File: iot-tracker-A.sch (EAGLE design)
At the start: 24 parts, among them IC1 ESP-WROOM-02, IC2 TPS610986DSER, U1 TPL5111DDCR

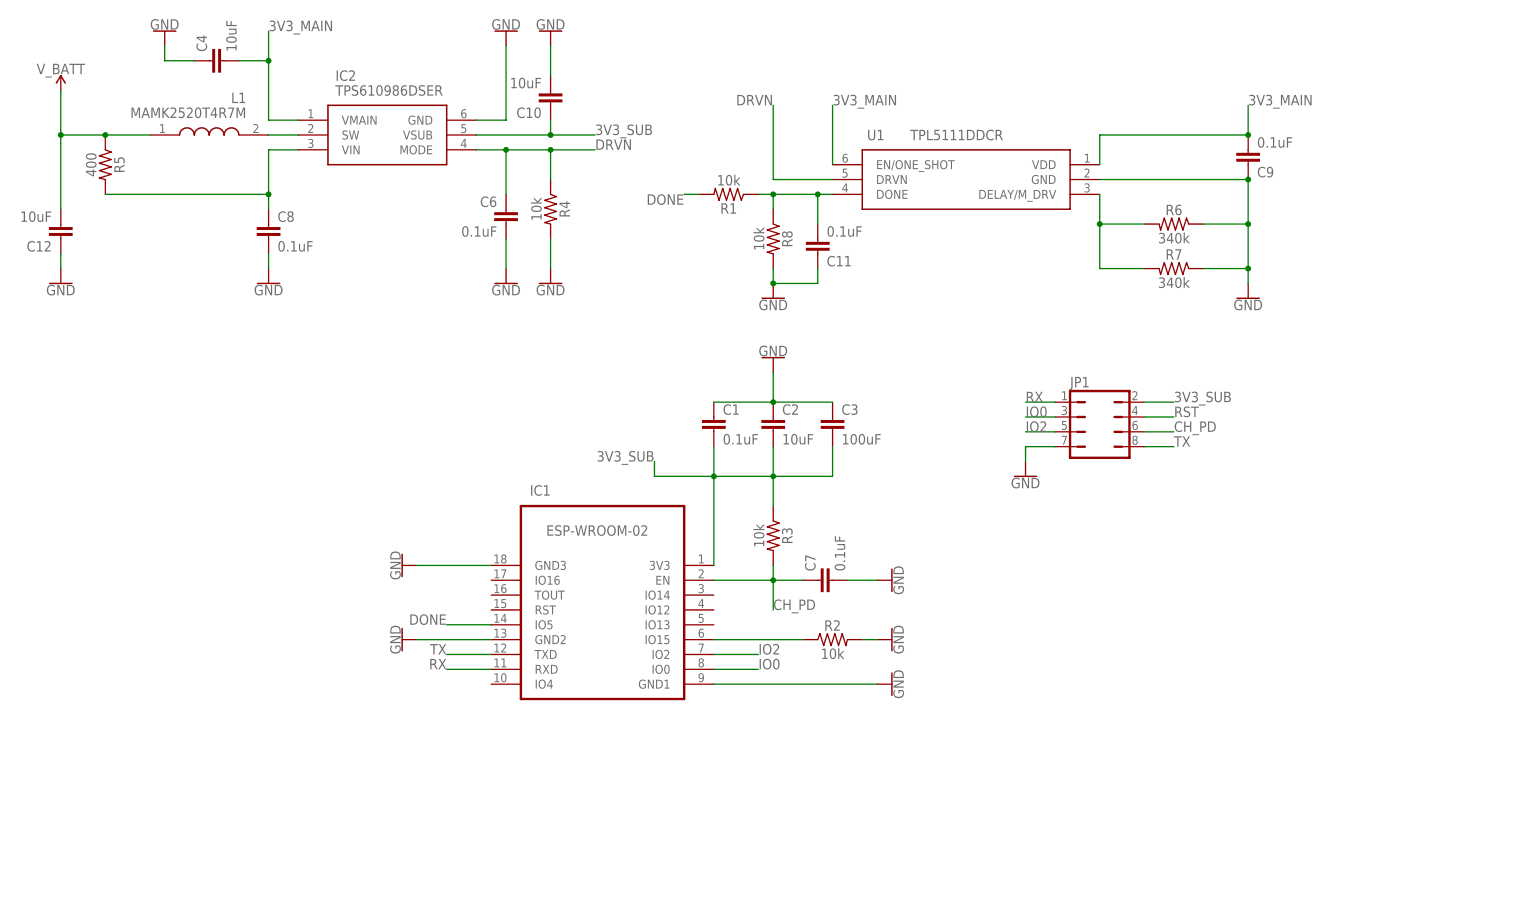
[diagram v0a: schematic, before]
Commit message: Added LED to GPIO4.
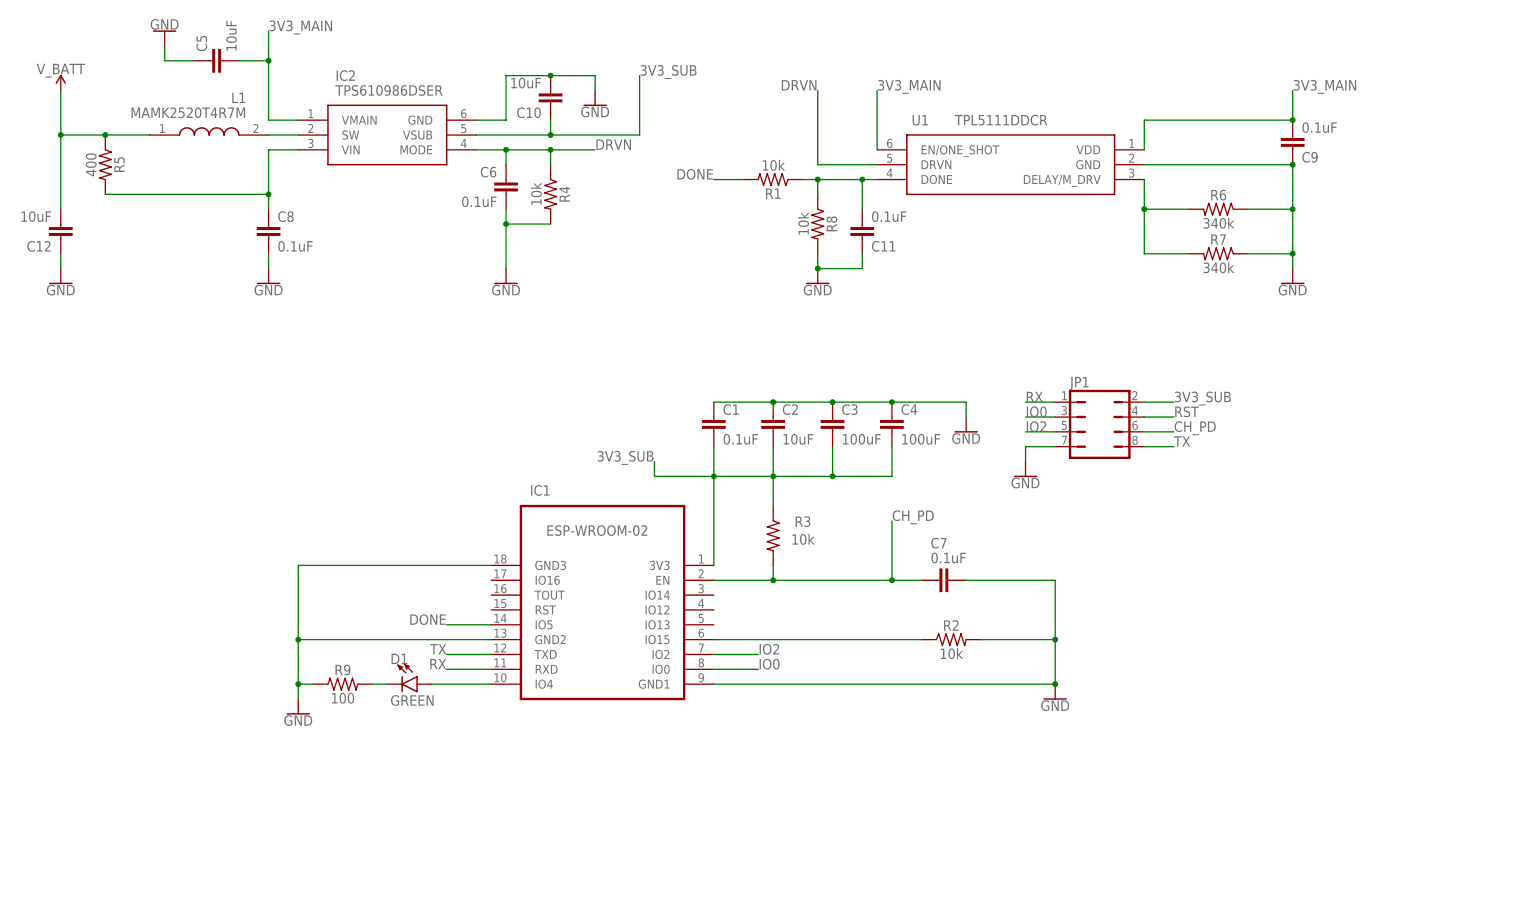
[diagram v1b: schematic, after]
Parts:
- added C5: 10uF, SparkFun-Capacitors:10UF-0603-6.3V-20%
- added D1: GREEN, SparkFun-LED:LED-GREEN0603
- added R9: 100, SparkFun-Resistors:100OHM-0603-1/10W-1%
- C4: value 10uF -> 100uF; device SparkFun-Capacitors:10UF-0603-6.3V-20% -> SparkFun-Capacitors:10UF-1206-6.3V-20%
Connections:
- new net N$2: D1.A, IC1.IO4
- new net N$5: D1.C, R9.2
- net 3V3_MAIN: now also C5.2; no longer C4.2
- net 3V3_SUB: now also C4.2
- net CH_PD: now also C7.2; no longer C7.1
- net GND: now also C5.1, C7.1, R9.1; no longer C7.2
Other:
- moved on the sheet: C11, C4, C6, C7, C9, R1, R2, R4, R6, R7, R8, U1

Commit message: Replaced TPS610986 with MCP1640 boost converter
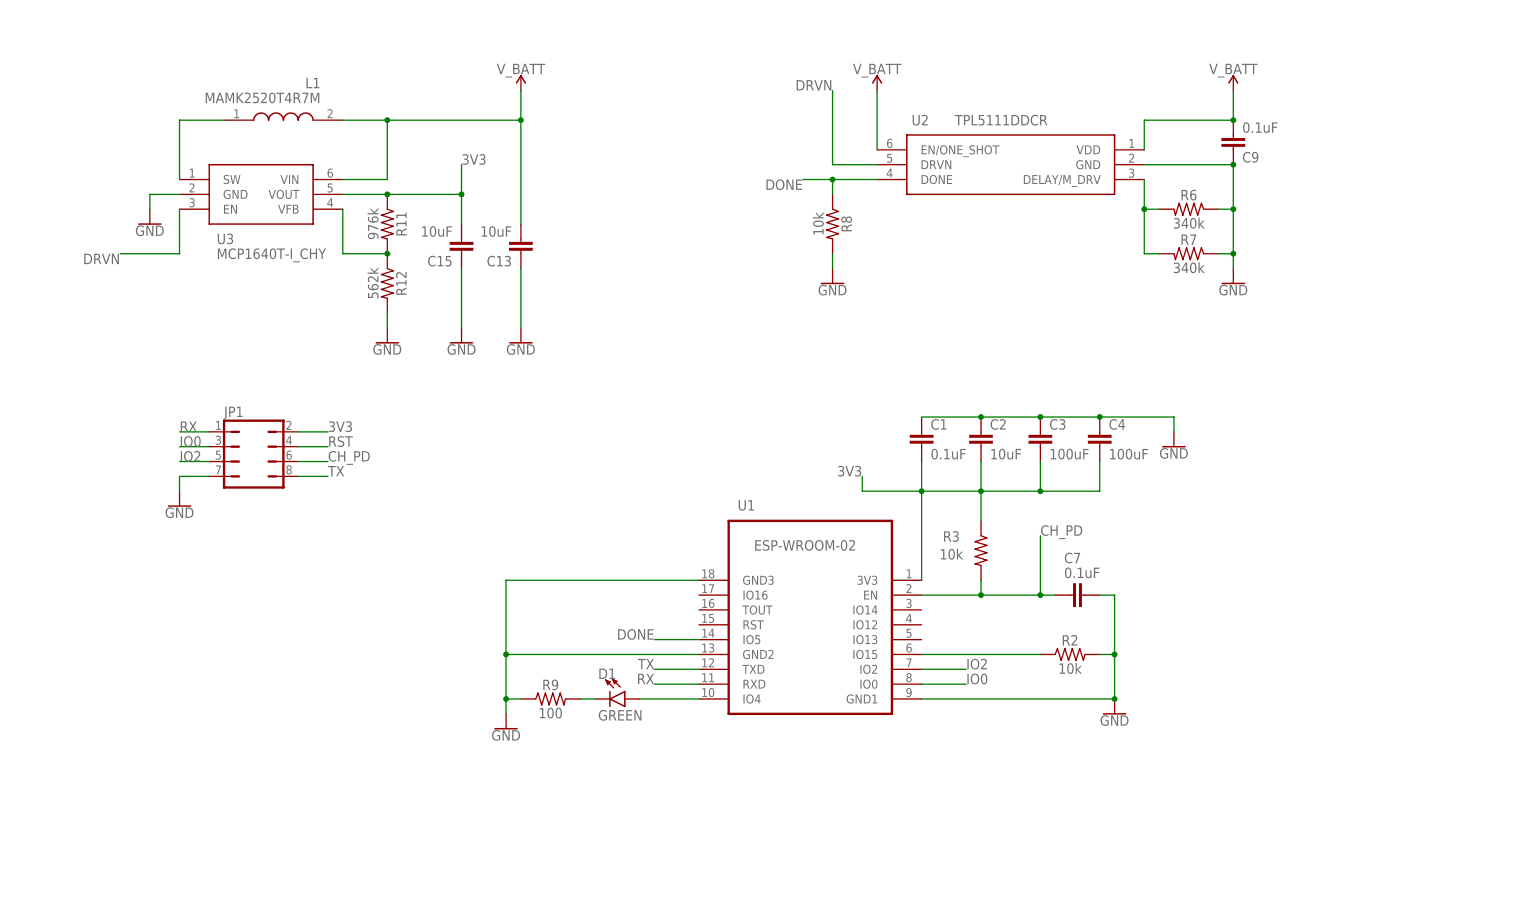
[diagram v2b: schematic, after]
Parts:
- removed C10, C12, C5: 10uF, SparkFun-Capacitors:10UF-0603-6.3V-20%
- removed C11, C6, C8: 0.1uF, SparkFun-Capacitors:0.1UF-0603-25V-(+80/-20%)
- removed IC1: ESP-WROOM-02, esp-wroom-02:ESP-WROOM-02
- removed IC2: TPS610986DSER, TPS610986DSER:TPS610986DSER
- removed R1, R4: 10k, SparkFun-Resistors:10KOHM-0603-1/10W-1%
- removed R5: 400, SparkFun-Resistors:10KOHM-0603-1/10W-1%
- added C13, C15: 10uF, SparkFun-Capacitors:10UF-0603-6.3V-20%
- added R11: 976k, SparkFun-Resistors:680OHM-0603-1/10W-5%
- added R12: 562k, SparkFun-Resistors:680OHM-0603-1/10W-5%
- added U2: TPL5111DDCR, TPL5111DDCR:TPL5111DDCR
- added U3: MCP1640T-I_CHY, MCP1640T-I_CHY:MCP1640T-I_CHY
- U1: value TPL5111DDCR -> ESP-WROOM-02; device TPL5111DDCR:TPL5111DDCR -> esp-wroom-02:ESP-WROOM-02
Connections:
- removed net 3V3_MAIN: C5.2, C9.2, IC2.VMAIN, U1.EN/ONE_SHOT, U1.VDD
- removed net 3V3_SUB: C1.2, C10.1, C2.2, C3.2, C4.2, IC1.3V3, IC2.VSUB, JP1.2, R3.1
- removed net N$4: IC2.SW, L1.2
- removed net N$6: C8.1, IC2.VIN, R5.2
- new net 3V3: C1.2, C15.2, C2.2, C3.2, C4.2, JP1.2, R11.1, R3.1, U1.3V3, U3.VOUT
- new net N$10: R11.2, R12.1, U3.VFB
- new net N$7: L1.1, U3.SW
- net CH_PD: now also U1.EN; no longer IC1.EN
- net DONE: now also U1.IO5, U2.DONE; no longer C11.2, IC1.IO5, R1.1, R1.2, U1.DONE
- net DRVN: now also U2.DRVN, U3.EN; no longer C6.1, IC2.MODE, R4.1, U1.DRVN
- net GND: now also C13.1, C15.1, R12.2, U1.GND0, U1.GND1, U1.GND2, U1.GND3, U2.GND, U3.GND; no longer C10.2, C11.1, C12.1, C5.1, C6.2, C8.2, IC1.GND0, IC1.GND1, IC1.GND2, IC1.GND3, IC2.GND, R4.2, U1.GND
- net IO0: now also U1.IO0; no longer IC1.IO0
- net IO2: now also U1.IO2; no longer IC1.IO2
- net N$1: now also U2.DELAY/M_DRV; no longer U1.DELAY/M_DRV
- net N$2: now also U1.IO4; no longer IC1.IO4
- net N$3: now also U1.IO15; no longer IC1.IO15
- net RX: now also U1.RXD; no longer IC1.RXD
- net TX: now also U1.TXD; no longer IC1.TXD
- net V_BATT: now also C13.2, C9.2, L1.2, U2.EN/ONE_SHOT, U2.VDD, U3.VIN; no longer C12.2, L1.1, R5.1
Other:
- moved on the sheet: C1, C2, C3, C4, C7, C9, D1, JP1, L1, R2, R3, R6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

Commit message: Reordered component names and added 3.3V symbol
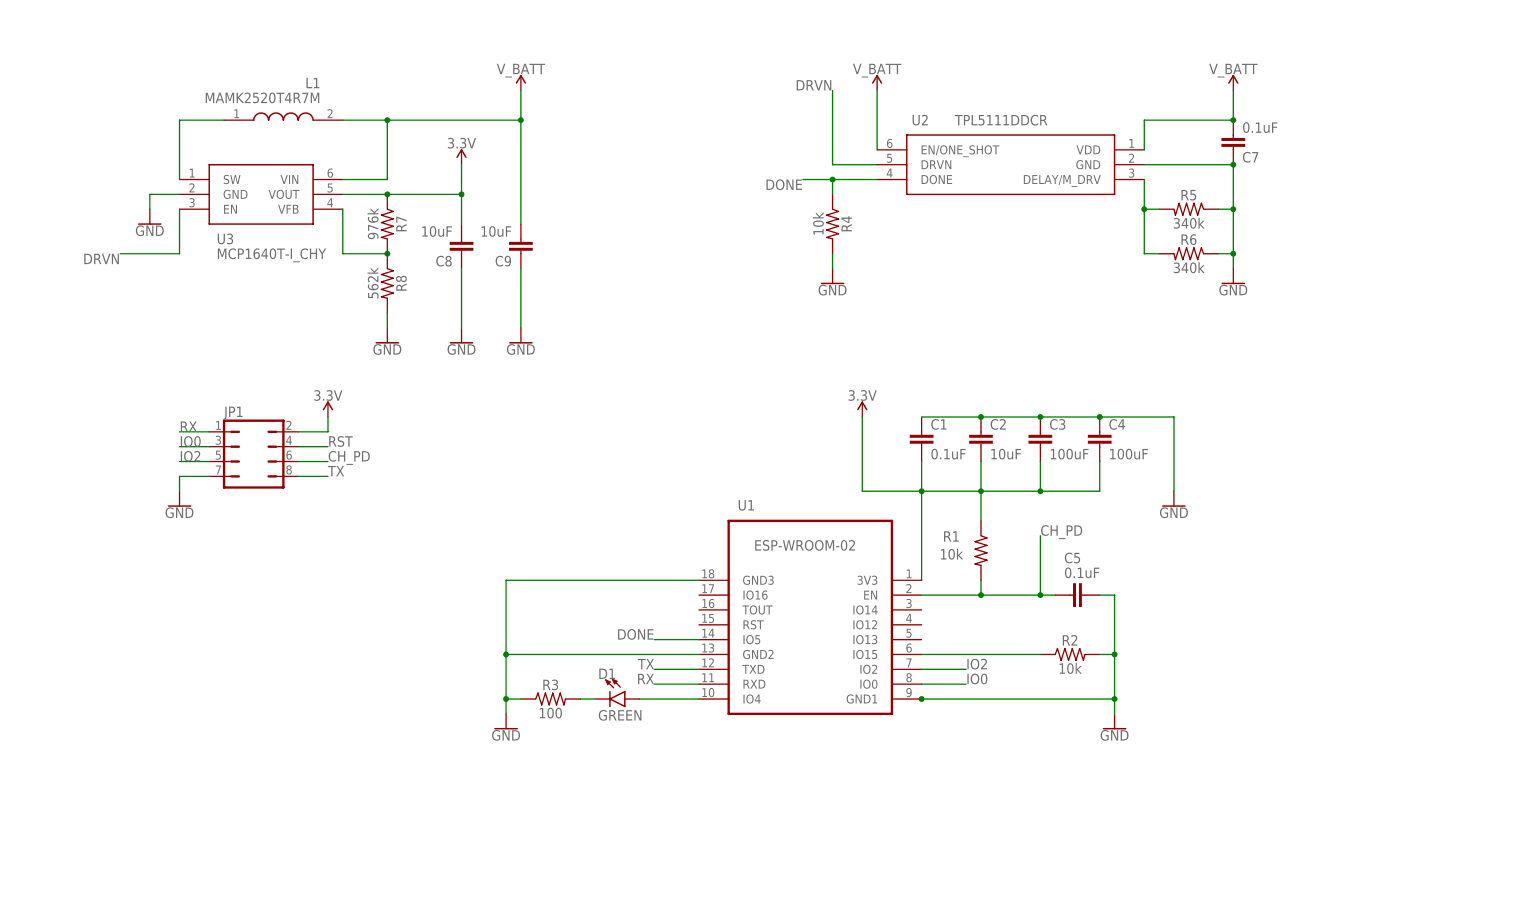
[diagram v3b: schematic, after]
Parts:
- removed C13: 10uF, SparkFun-Capacitors:10UF-0603-6.3V-20%
- removed R11: 976k, SparkFun-Resistors:680OHM-0603-1/10W-5%
- removed R12: 562k, SparkFun-Resistors:680OHM-0603-1/10W-5%
- removed R9: 100, SparkFun-Resistors:100OHM-0603-1/10W-1%
- added C5: 0.1uF, SparkFun-Capacitors:0.1UF-0603-25V-(+80/-20%)
- added R1, R4: 10k, SparkFun-Resistors:10KOHM-0603-1/10W-1%
- added R5: 340k, SparkFun-Resistors:330KOHM-0603-1/10W-1%
- C9: value 0.1uF -> 10uF; device SparkFun-Capacitors:0.1UF-0603-25V-(+80/-20%) -> SparkFun-Capacitors:10UF-0603-6.3V-20%
- R3: value 10k -> 100; device SparkFun-Resistors:10KOHM-0603-1/10W-1% -> SparkFun-Resistors:100OHM-0603-1/10W-1%
- R7: value 340k -> 976k; device SparkFun-Resistors:330KOHM-0603-1/10W-1% -> SparkFun-Resistors:680OHM-0603-1/10W-5%
- R8: value 10k -> 562k; device SparkFun-Resistors:10KOHM-0603-1/10W-1% -> SparkFun-Resistors:680OHM-0603-1/10W-5%
- renumbered C15 to C8
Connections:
- removed net 3V3: C1.2, C2.2, C3.2, C4.2, C8.2, JP1.2, R11.1, R3.1, U1.3V3, U3.VOUT
- new net 3.3V: C1.2, C2.2, C3.2, C4.2, C8.2, JP1.2, R1.1, R7.1, U1.3V3, U3.VOUT
- net CH_PD: now also C5.2, R1.2; no longer C7.2, R3.2
- net DONE: now also R4.1; no longer R8.1
- net GND: now also C5.1, R3.1, R4.2, R5.1; no longer C13.1, R12.2, R7.1, R9.1
- net N$1: now also R5.2; no longer R7.2
- net N$10: now also R7.2, R8.1; no longer R11.2, R12.1
- net N$5: now also R3.2; no longer R9.2
- net V_BATT: now also C7.2; no longer C13.2
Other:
- moved on the sheet: C7, C9, R3, R6, R7, R8

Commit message: Created the board file
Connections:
- net N$1 renamed DELAY
- net N$10 renamed VFB
- net N$2 renamed IO4_LED
- net N$3 renamed IO15
- net N$5 renamed LED_GND
- net N$7 renamed SW
- net 3.3V: now also JP1.7; no longer JP1.2
- net CH_PD: now also JP1.3; no longer JP1.6
- net GND: now also JP1.2; no longer JP1.7
- net IO0: now also JP1.6; no longer JP1.3
- net IO2: now also JP1.4; no longer JP1.5
- net RST: now also JP1.5; no longer JP1.4
- net RX: now also JP1.8; no longer JP1.1
- net TX: now also JP1.1; no longer JP1.8
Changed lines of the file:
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@@
 <attribute name="VALUE" x="-116.84" y="8.255" size="1.778" layer="96"/>
 </instance>
-<instance part="GND1" gate="1" x="-124.46" y="7.62" smashed="yes">
-<attribute name="VALUE" x="-124.46" y="7.366" size="1.778" layer="96" align="top-center"/>
+<instance part="GND1" gate="1" x="-83.82" y="17.78" smashed="yes">
+<attribute name="VALUE" x="-83.82" y="17.526" size="1.778" layer="96" align="top-center"/>
 </instance>
 <instance part="GND8" gate="1" x="-68.58" y="-30.48" smashed="yes">
@@
 <attribute name="VALUE" x="-7.62" y="25.654" size="1.778" layer="96" align="bottom-center"/>
 </instance>
-<instance part="SUPPLY6" gate="G$1" x="-99.06" y="22.86" smashed="yes">
-<attribute name="VALUE" x="-99.06" y="25.654" size="1.778" layer="96" align="bottom-center"/>
+<instance part="SUPPLY6" gate="G$1" x="-137.16" y="12.7" smashed="yes">
+<attribute name="VALUE" x="-137.16" y="15.494" size="1.778" layer="96" align="bottom-center"/>
 </instance>
 </instances>
@@
 </segment>
 <segment>
-<pinref part="GND1" gate="1" pin="GND"/>
-<pinref part="JP1" gate="B" pin="7"/>
-<wire x1="-124.46" y1="10.16" x2="-124.46" y2="12.7" width="0.1524" layer="91"/>
-<wire x1="-124.46" y1="12.7" x2="-119.38" y2="12.7" width="0.1524" layer="91"/>
-</segment>
-<segment>
 <wire x1="2.54" y1="22.86" x2="12.7" y2="22.86" width="0.1524" layer="91"/>
 <junction x="12.7" y="22.86"/>
@@
 <wire x1="-66.04" y1="48.26" x2="-66.04" y2="38.1" width="0.1524" layer="91"/>
 </segment>
+<segment>
+<pinref part="JP1" gate="B" pin="2"/>
+<pinref part="GND1" gate="1" pin="GND"/>
+<wire x1="-104.14" y1="20.32" x2="-83.82" y2="20.32" width="0.1524" layer="91"/>
+</segment>
 </net>
 <net name="DONE" class="0">
@@
 </segment>
 </net>
-<net name="N$3" class="0">
+<net name="IO15" class="0">
 <segment>
 <pinref part="U1" gate="G$1" pin="IO15"/>
@@
 <net name="RX" class="0">
 <segment>
-<pinref part="JP1" gate="B" pin="1"/>
-<wire x1="-119.38" y1="20.32" x2="-124.46" y2="20.32" width="0.1524" layer="91"/>
-<label x="-124.46" y="20.32" size="1.778" layer="95"/>
-</segment>
-<segment>
 <pinref part="U1" gate="G$1" pin="RXD"/>
 <wire x1="-35.56" y1="-22.86" x2="-43.18" y2="-22.86" width="0.1524" layer="91"/>
 <label x="-43.18" y="-22.86" size="1.778" layer="95" rot="MR0"/>
 </segment>
-</net>
-<net name="TX" class="0">
 <segment>
 <pinref part="JP1" gate="B" pin="8"/>
@@
 <label x="-99.06" y="12.7" size="1.778" layer="95"/>
 </segment>
+</net>
+<net name="TX" class="0">
 <segment>
 <pinref part="U1" gate="G$1" pin="TXD"/>
@@
 <label x="-43.18" y="-20.32" size="1.778" layer="95" rot="MR0"/>
 </segment>
+<segment>
+<pinref part="JP1" gate="B" pin="1"/>
+<wire x1="-119.38" y1="20.32" x2="-124.46" y2="20.32" width="0.1524" layer="91"/>
+<label x="-124.46" y="20.32" size="1.778" layer="95" rot="R180"/>
+</segment>
 </net>
 <net name="IO0" class="0">
-<segment>
-<pinref part="JP1" gate="B" pin="3"/>
-<wire x1="-119.38" y1="17.78" x2="-124.46" y2="17.78" width="0.1524" layer="91"/>
-<label x="-124.46" y="17.78" size="1.778" layer="95"/>
-</segment>
 <segment>
 <pinref part="U1" gate="G$1" pin="IO0"/>
@@
 <label x="10.16" y="-22.86" size="1.778" layer="95"/>
 </segment>
+<segment>
+<pinref part="JP1" gate="B" pin="6"/>
+<wire x1="-104.14" y1="15.24" x2="-99.06" y2="15.24" width="0.1524" layer="91"/>
+<label x="-99.06" y="15.24" size="1.778" layer="95"/>
+</segment>
 </net>
 <net name="IO2" class="0">
-<segment>
-<pinref part="JP1" gate="B" pin="5"/>
-<wire x1="-119.38" y1="15.24" x2="-124.46" y2="15.24" width="0.1524" layer="91"/>
-<label x="-124.46" y="15.24" size="1.778" layer="95"/>
-</segment>
 <segment>
 <pinref part="U1" gate="G$1" pin="IO2"/>
@@
 <label x="10.16" y="-20.32" size="1.778" layer="95"/>
 </segment>
-</net>
-<net name="RST" class="0">
 <segment>
 <pinref part="JP1" gate="B" pin="4"/>
@@
 </net>
 <net name="CH_PD" class="0">
-<segment>
-<pinref part="JP1" gate="B" pin="6"/>
-<wire x1="-104.14" y1="15.24" x2="-99.06" y2="15.24" width="0.1524" layer="91"/>
-<label x="-99.06" y="15.24" size="1.778" layer="95"/>
-</segment>
 <segment>
 <pinref part="U1" gate="G$1" pin="EN"/>
@@
 <label x="22.86" y="2.54" size="1.778" layer="95"/>
 </segment>
-</net>
-<net name="N$1" class="0">
+<segment>
+<pinref part="JP1" gate="B" pin="3"/>
+<wire x1="-119.38" y1="17.78" x2="-124.46" y2="17.78" width="0.1524" layer="91"/>
+<label x="-124.46" y="17.78" size="1.778" layer="95" rot="R180"/>
+</segment>
+</net>
+<net name="DELAY" class="0">
 <segment>
 <pinref part="U2" gate="G$1" pin="DELAY/M_DRV"/>
@@
 </segment>
 <segment>
-<pinref part="JP1" gate="B" pin="2"/>
-<wire x1="-104.14" y1="20.32" x2="-99.06" y2="20.32" width="0.1524" layer="91"/>
-<pinref part="SUPPLY6" gate="G$1" pin="3.3V"/>
-<wire x1="-99.06" y1="20.32" x2="-99.06" y2="22.86" width="0.1524" layer="91"/>
-</segment>
-<segment>
 <pinref part="U3" gate="G$1" pin="VOUT"/>
 <pinref part="R7" gate="G$1" pin="1"/>
@@
 <wire x1="-76.2" y1="66.04" x2="-76.2" y2="60.96" width="0.1524" layer="91"/>
 <junction x="-76.2" y="60.96"/>
+</segment>
+<segment>
+<pinref part="SUPPLY6" gate="G$1" pin="3.3V"/>
+<pinref part="JP1" gate="B" pin="7"/>
+<wire x1="-137.16" y1="12.7" x2="-119.38" y2="12.7" width="0.1524" layer="91"/>
 </segment>
 </net>
@@
 </segment>
 </net>
-<net name="N$2" class="0">
+<net name="IO4_LED" class="0">
 <segment>
 <pinref part="U1" gate="G$1" pin="IO4"/>
@@
 </segment>
 </net>
-<net name="N$5" class="0">
+<net name="LED_GND" class="0">
 <segment>
 <pinref part="R3" gate="G$1" pin="2"/>
@@
 </segment>
 </net>
-<net name="N$7" class="0">
+<net name="SW" class="0">
 <segment>
 <pinref part="U3" gate="G$1" pin="SW"/>
@@
 </segment>
 </net>
-<net name="N$10" class="0">
+<net name="VFB" class="0">
 <segment>
 <pinref part="R7" gate="G$1" pin="2"/>
@@
 </segment>
 </net>
+<net name="RST" class="0">
+<segment>
+<pinref part="JP1" gate="B" pin="5"/>
+<wire x1="-119.38" y1="15.24" x2="-124.46" y2="15.24" width="0.1524" layer="91"/>
+<label x="-124.46" y="15.24" size="1.778" layer="95" rot="R180"/>
+</segment>
+</net>
